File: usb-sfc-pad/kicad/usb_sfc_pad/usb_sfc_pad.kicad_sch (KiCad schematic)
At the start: 36 parts, among them IC101 PIC16F1459-ISS, J101 532610671, J102 532610271, J102 HEADER_6P-2.54, J103 532610271, J104 532610271, J105 532610271, SW101 SW_Pad, SW102 SW_Pad, SW103 SW_Pad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

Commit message: Add footprint SFC_Pad
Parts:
- SW101, SW102, SW103, SW104, SW105, SW106, SW107, SW108, SW109, SW110, SW111, SW112: footprint (none) -> Local:SFC_Pad_F_NoSolder_5.5mm
- renumbered J102 to J103, J103 to J104, J104 to J105, J105 to J106
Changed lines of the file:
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@@
 			)
 		)
-		(property "Footprint" ""
+		(property "Footprint" "Local:SFC_Pad_F_NoSolder_5.5mm"
 			(at 73.66 123.19 0)
 			(effects
@@
 			)
 		)
-		(property "Footprint" ""
+		(property "Footprint" "Local:SFC_Pad_F_NoSolder_5.5mm"
 			(at 110.49 123.19 0)
 			(effects
@@
 		(on_board yes)
 		(dnp no)
-		(property "Reference" "J105"
+		(property "Reference" "J106"
 			(at 256.032 118.364 90)
 			(effects
@@
 			(project "usb_sfc_pad"
 				(path "/7a50d412-cc3f-49bd-9754-262bb19f947d"
-					(reference "J105")
+					(reference "J106")
 					(unit 1)
 				)
@@
 		(on_board yes)
 		(dnp no)
-		(property "Reference" "J104"
+		(property "Reference" "J105"
 			(at 235.712 118.11 90)
 			(effects
@@
 			(project "usb_sfc_pad"
 				(path "/7a50d412-cc3f-49bd-9754-262bb19f947d"
-					(reference "J104")
+					(reference "J105")
 					(unit 1)
 				)
@@
 			)
 		)
-		(property "Footprint" ""
+		(property "Footprint" "Local:SFC_Pad_F_NoSolder_5.5mm"
 			(at 190.5 97.79 0)
 			(effects
@@
 			)
 		)
-		(property "Footprint" ""
+		(property "Footprint" "Local:SFC_Pad_F_NoSolder_5.5mm"
 			(at 38.1 123.19 0)
 			(effects
@@
 			)
 		)
-		(property "Footprint" ""
+		(property "Footprint" "Local:SFC_Pad_F_NoSolder_5.5mm"
 			(at 73.66 166.37 0)
 			(effects
@@
 		(on_board yes)
 		(dnp no)
-		(property "Reference" "J102"
+		(property "Reference" "J103"
 			(at 236.982 68.58 90)
 			(effects
@@
 			(project ""
 				(path "/7a50d412-cc3f-49bd-9754-262bb19f947d"
-					(reference "J102")
+					(reference "J103")
 					(unit 1)
 				)
@@
 			)
 		)
-		(property "Footprint" ""
+		(property "Footprint" "Local:SFC_Pad_F_NoSolder_5.5mm"
 			(at 260.35 93.98 0)
 			(effects
@@
 			)
 		)
-		(property "Footprint" ""
+		(property "Footprint" "Local:SFC_Pad_F_NoSolder_5.5mm"
 			(at 147.32 166.37 0)
 			(effects
@@
 			)
 		)
-		(property "Footprint" ""
+		(property "Footprint" "Local:SFC_Pad_F_NoSolder_5.5mm"
 			(at 38.1 166.37 0)
 			(effects
@@
 			)
 		)
-		(property "Footprint" ""
+		(property "Footprint" "Local:SFC_Pad_F_NoSolder_5.5mm"
 			(at 110.49 166.37 0)
 			(effects
@@
 		(on_board yes)
 		(dnp no)
-		(property "Reference" "J103"
+		(property "Reference" "J104"
 			(at 257.302 68.834 90)
 			(effects
@@
 			(project "usb_sfc_pad"
 				(path "/7a50d412-cc3f-49bd-9754-262bb19f947d"
-					(reference "J103")
+					(reference "J104")
 					(unit 1)
 				)
@@
 			)
 		)
-		(property "Footprint" ""
+		(property "Footprint" "Local:SFC_Pad_F_NoSolder_5.5mm"
 			(at 147.32 123.19 0)
 			(effects
@@
 			)
 		)
-		(property "Footprint" ""
+		(property "Footprint" "Local:SFC_Pad_F_NoSolder_5.5mm"
 			(at 190.5 140.97 0)
 			(effects
@@
 			)
 		)
-		(property "Footprint" ""
+		(property "Footprint" "Local:SFC_Pad_F_NoSolder_5.5mm"
 			(at 259.08 143.51 0)
 			(effects

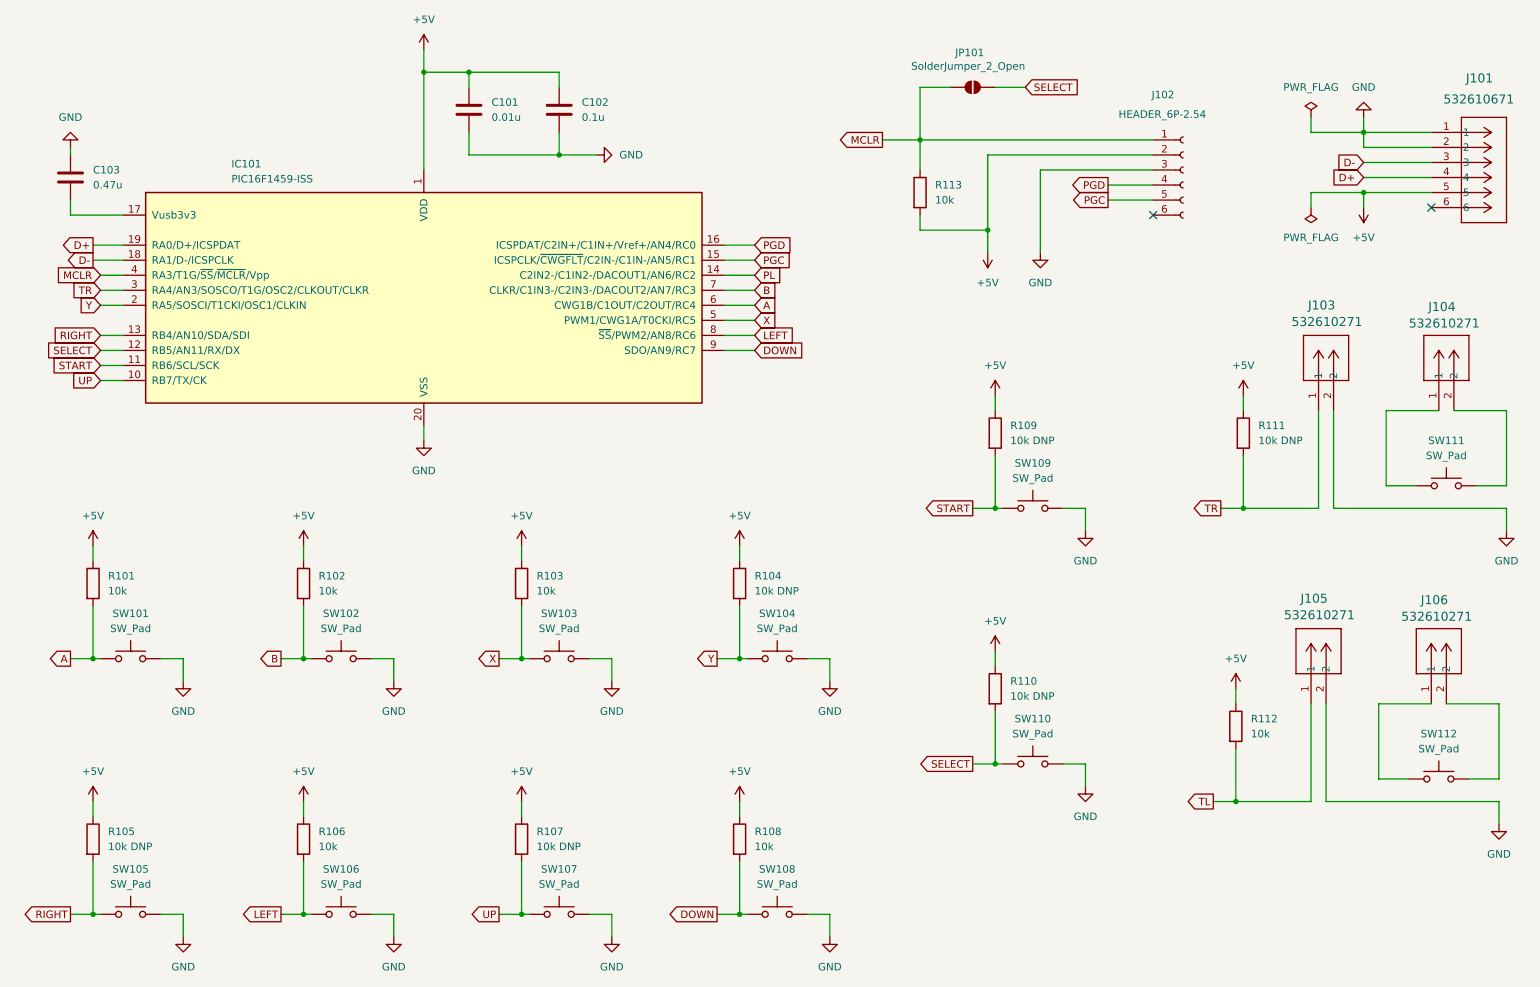
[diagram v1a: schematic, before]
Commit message: Add PCB
- Renumber SFC_Pad's pins
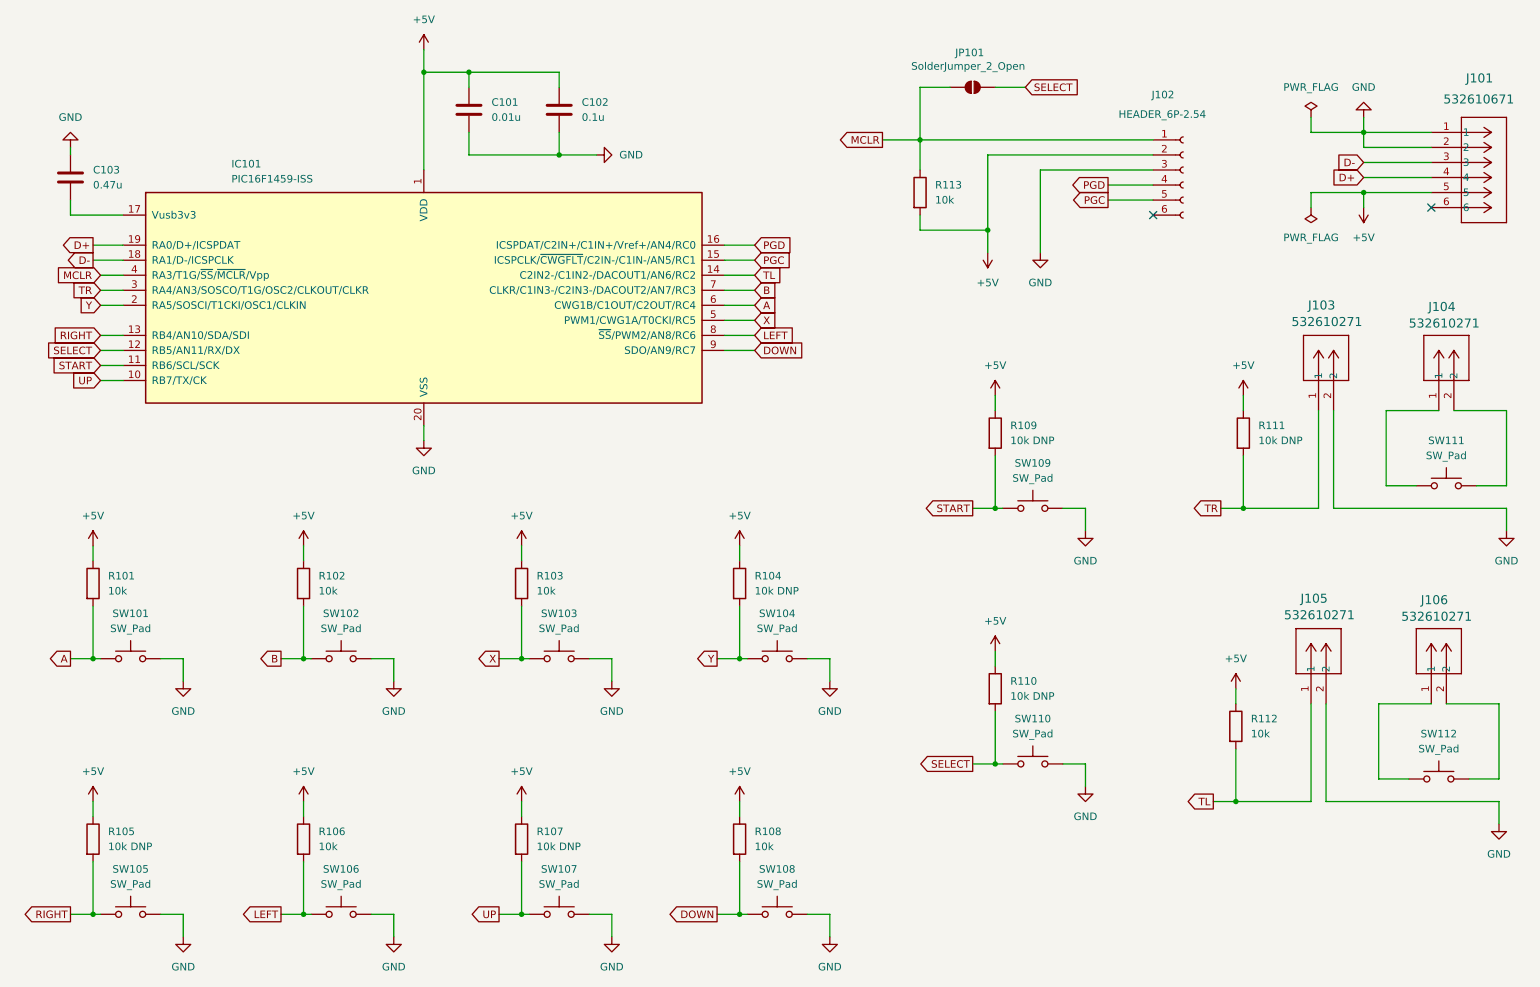
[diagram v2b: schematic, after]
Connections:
- net PL is gone; now on net TL: IC101.14 (C2IN2-/C1IN2-/DACOUT1/AN6/RC2)
- net A: now also SW101.2; no longer SW101.1
- net B: now also SW102.2; no longer SW102.1
- net GND: now also SW101.1, SW102.1, SW103.1, SW104.1, SW106.1; no longer SW101.2, SW102.2, SW103.2, SW104.2, SW106.2
- net LEFT: now also SW106.2; no longer SW106.1
- net X: now also SW103.2; no longer SW103.1
- net Y: now also SW104.2; no longer SW104.1
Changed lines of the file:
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@@
 		)
 	)
-	(global_label "PL"
+	(global_label "TL"
 		(shape input)
 		(at 143.51 63.5 0)
@@
 		)
 		(property "Intersheetrefs" "${INTERSHEET_REFS}"
-			(at 148.7933 63.5 0)
+			(at 148.4909 63.5 0)
 			(effects
 				(font
@@
 		(lib_id "Local:SW_Pad")
 		(at 73.66 128.27 0)
+		(mirror y)
 		(unit 1)
 		(exclude_from_sim no)
@@
 		(on_board yes)
 		(dnp no)
-		(fields_autoplaced yes)
 		(property "Reference" "SW102"
 			(at 73.66 120.65 0)
@@
 		(lib_id "Local:SW_Pad")
 		(at 110.49 128.27 0)
+		(mirror y)
 		(unit 1)
 		(exclude_from_sim no)
@@
 		(on_board yes)
 		(dnp no)
-		(fields_autoplaced yes)
 		(property "Reference" "SW103"
 			(at 110.49 120.65 0)
@@
 		(lib_id "Local:SW_Pad")
 		(at 38.1 128.27 0)
+		(mirror y)
 		(unit 1)
 		(exclude_from_sim no)
@@
 		(on_board yes)
 		(dnp no)
-		(fields_autoplaced yes)
 		(property "Reference" "SW101"
 			(at 38.1 120.65 0)
@@
 		(lib_id "Local:SW_Pad")
 		(at 73.66 171.45 0)
+		(mirror y)
 		(unit 1)
 		(exclude_from_sim no)
@@
 		(on_board yes)
 		(dnp no)
-		(fields_autoplaced yes)
 		(property "Reference" "SW106"
 			(at 73.66 163.83 0)
@@
 		(on_board yes)
 		(dnp no)
-		(fields_autoplaced yes)
 		(property "Reference" "SW108"
 			(at 147.32 163.83 0)
@@
 		(on_board yes)
 		(dnp no)
-		(fields_autoplaced yes)
 		(property "Reference" "SW105"
 			(at 38.1 163.83 0)
@@
 		(on_board yes)
 		(dnp no)
-		(fields_autoplaced yes)
 		(property "Reference" "SW107"
 			(at 110.49 163.83 0)
@@
 		(lib_id "Local:SW_Pad")
 		(at 147.32 128.27 0)
+		(mirror y)
 		(unit 1)
 		(exclude_from_sim no)
@@
 		(on_board yes)
 		(dnp no)
-		(fields_autoplaced yes)
 		(property "Reference" "SW104"
 			(at 147.32 120.65 0)

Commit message: Fix clearance in IC101 pads
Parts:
- IC101: footprint Package_SO:SSOP-20_5.3x7.2mm_P0.65mm -> Local:SSOP-20_5.3x7.2mm_P0.65mm
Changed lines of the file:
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@@
 			)
 		)
-		(property "Footprint" "Package_SO:SSOP-20_5.3x7.2mm_P0.65mm"
+		(property "Footprint" "Local:SSOP-20_5.3x7.2mm_P0.65mm"
 			(at 87.63 63.5 0)
 			(effects

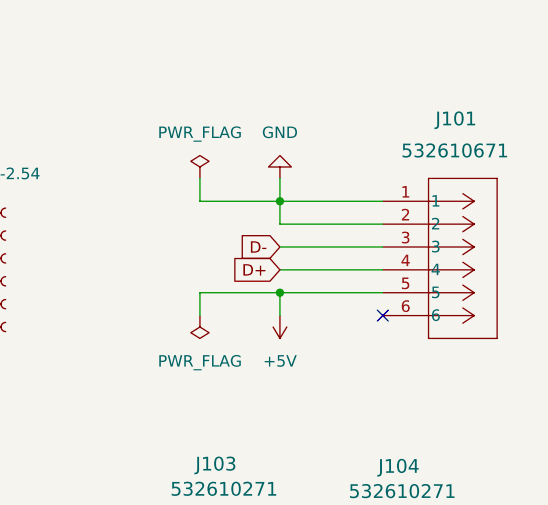
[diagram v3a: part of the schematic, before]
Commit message: Replace 532610671 with 532610571
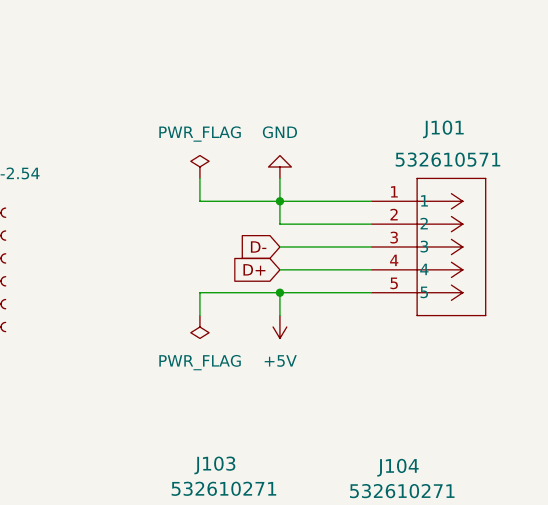
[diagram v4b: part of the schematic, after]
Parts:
- removed J101: 532610671, Local:CONN_532610001-SD_06_MOL, symbol Local:532610671
- added J101: 532610571, Local:CONN_532610001-SD_05_MOL, symbol Local:532610571
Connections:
- net +5V: now also J101.5
- net D+: now also J101.4
- net D-: now also J101.3
- net GND: now also J101.1, J101.2
- no-connect marks 2 -> 1
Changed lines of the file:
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@@
 		(at 210.82 53.34)
 	)
-	(no_connect
-		(at 257.81 52.07)
-	)
 	(wire
 		(pts
@@
 	(wire
 		(pts
-			(xy 257.81 49.53) (xy 246.38 49.53)
+			(xy 246.38 49.53) (xy 256.54 49.53)
 		)
 		(stroke
@@
 	(wire
 		(pts
-			(xy 246.38 44.45) (xy 257.81 44.45)
+			(xy 246.38 44.45) (xy 256.54 44.45)
 		)
 		(stroke
@@
 	(wire
 		(pts
-			(xy 246.38 46.99) (xy 257.81 46.99)
+			(xy 246.38 46.99) (xy 256.54 46.99)
 		)
 		(stroke
@@
 	(wire
 		(pts
-			(xy 257.81 41.91) (xy 246.38 41.91)
+			(xy 246.38 41.91) (xy 256.54 41.91)
 		)
 		(stroke
@@
 	(wire
 		(pts
-			(xy 257.81 39.37) (xy 246.38 39.37)
+			(xy 246.38 39.37) (xy 256.54 39.37)
 		)
 		(stroke
@@
 	)
 	(symbol
+		(lib_id "Local:532610571")
+		(at 256.54 39.37 0)
+		(unit 1)
+		(exclude_from_sim no)
+		(in_bom yes)
+		(on_board yes)
+		(dnp no)
+		(property "Reference" "J101"
+			(at 262.382 31.242 0)
+			(effects
+				(font
+					(size 1.524 1.524)
+				)
+				(justify left)
+			)
+		)
+		(property "Value" "532610571"
+			(at 259.08 34.798 0)
+			(effects
+				(font
+					(size 1.524 1.524)
+				)
+				(justify left)
+			)
+		)
+		(property "Footprint" "Local:CONN_532610001-SD_05_MOL"
+			(at 264.414 54.356 0)
+			(effects
+				(font
+					(size 1.27 1.27)
+				)
+				(hide yes)
+			)
+		)
+		(property "Datasheet" "https://www.molex.com/en-us/products/part-detail-pdf/532610571?display=pdf"
+			(at 265.43 57.15 0)
+			(effects
+				(font
+					(size 1.27 1.27)
+				)
+				(hide yes)
+			)
+		)
+		(property "Description" ""
+			(at 256.54 39.37 0)
+			(effects
+				(font
+					(size 1.27 1.27)
+				)
+				(hide yes)
+			)
+		)
+		(pin "4"
+		)
+		(pin "5"
+		)
+		(pin "1"
+		)
+		(pin "3"
+		)
+		(pin "2"
+		)
+		(instances
+			(project ""
+				(path "/7a50d412-cc3f-49bd-9754-262bb19f947d"
+					(reference "J101")
+					(unit 1)
+				)
+			)
+		)
+	)
+	(symbol
 		(lib_id "power:GND")
 		(at 246.38 36.83 0)
@@
 					(unit 1)
 				)
-			)
-		)
-	)
-	(symbol
-		(lib_id "Local:532610671")
-		(at 257.81 39.37 0)
-		(unit 1)
-		(exclude_from_sim no)
-		(in_bom yes)
-		(on_board yes)
-		(dnp no)
-		(property "Reference" "J101"
-			(at 263.652 30.226 0)
-			(effects
-				(font
-					(size 1.524 1.524)
-				)
-				(justify left)
-			)
-		)
-		(property "Value" "532610671"
-			(at 259.842 33.782 0)
-			(effects
-				(font
-					(size 1.524 1.524)
-				)
-				(justify left)
-			)
-		)
-		(property "Footprint" "Local:CONN_532610001-SD_06_MOL"
-			(at 266.7 56.896 0)
-			(effects
-				(font
-					(size 1.27 1.27)
-					(italic yes)
-				)
-				(hide yes)
-			)
-		)
-		(property "Datasheet" "https://www.molex.com/en-us/products/part-detail-pdf/532610671?display=pdf"
-			(at 264.922 59.944 0)
-			(effects
-				(font
-					(size 1.27 1.27)
-					(italic yes)
-				)
-				(hide yes)
-			)
-		)
-		(property "Description" ""
-			(at 257.81 39.37 0)
-			(effects
-				(font
-					(size 1.27 1.27)
-				)
-				(hide yes)
-			)
-		)
-		(pin "1"
-		)
-		(pin "2"
-		)
-		(pin "5"
-		)
-		(pin "6"
-		)
-		(pin "3"
-		)
-		(pin "4"
-		)
-		(instances
-			(project ""
-				(path "/7a50d412-cc3f-49bd-9754-262bb19f947d"
-					(reference "J101")
-					(unit 1)
-				)

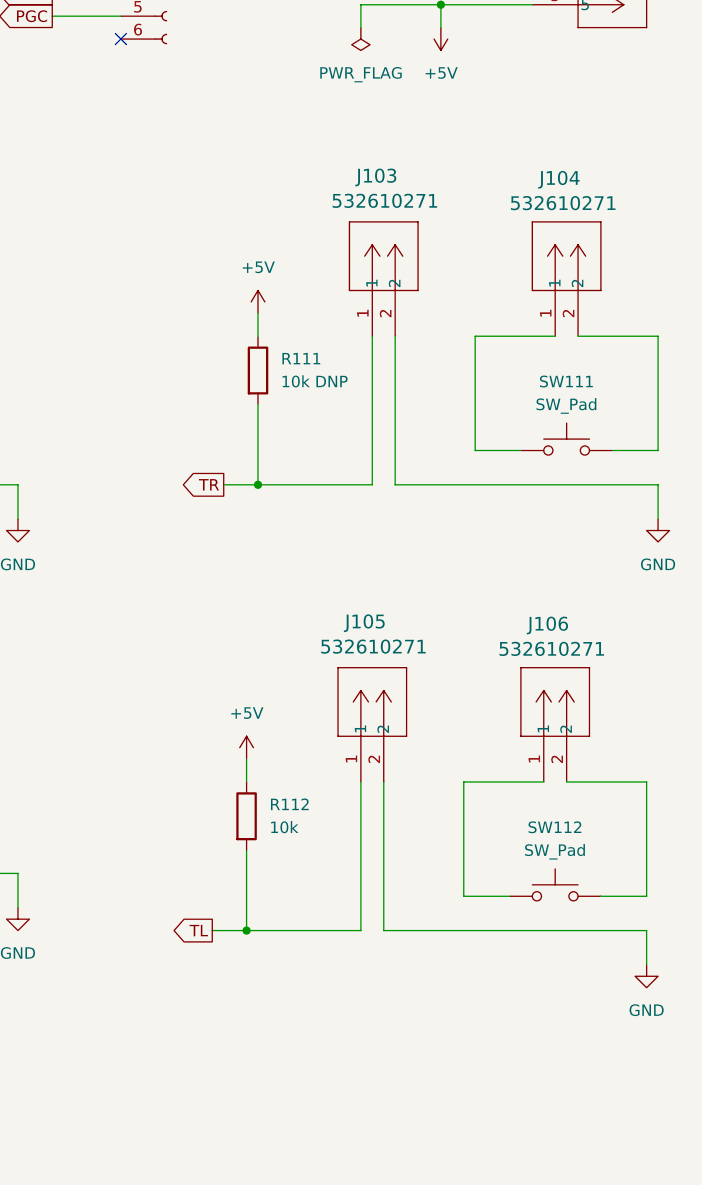
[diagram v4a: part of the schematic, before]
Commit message: Replace right-angle 2pins with vertical ones
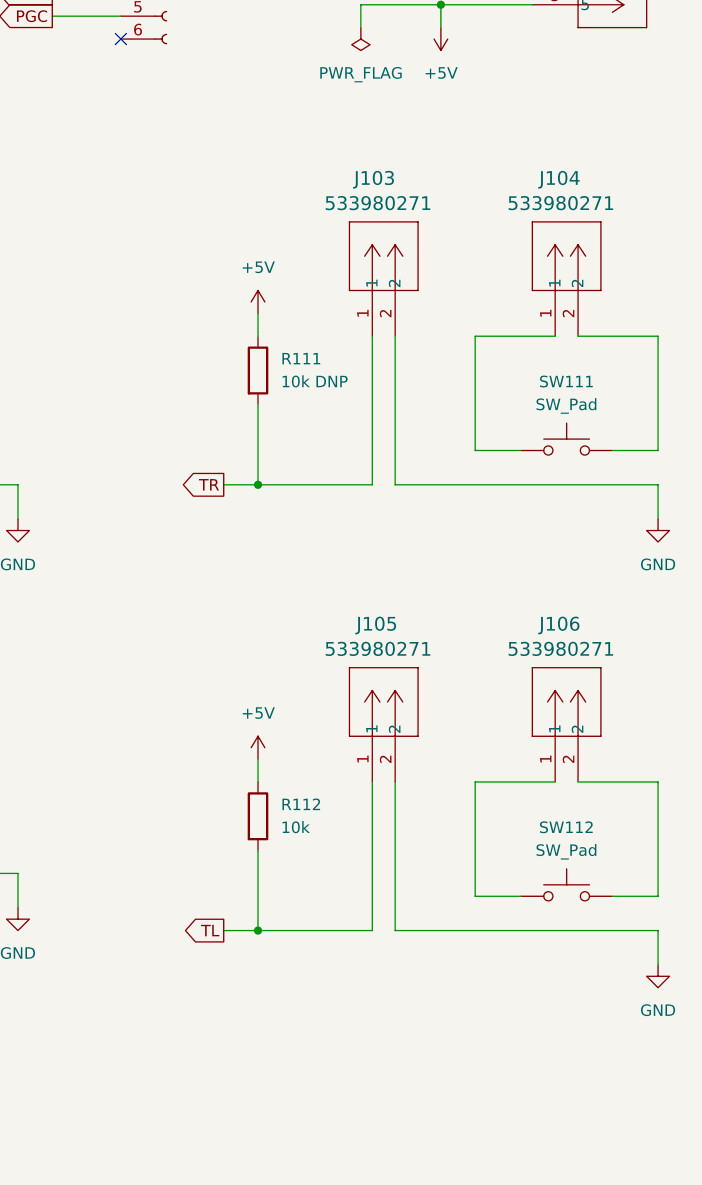
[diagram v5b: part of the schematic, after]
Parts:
- removed J103, J104, J105, J106: 532610271, Local:CONN_532610001-SD_02_MOL, symbol Local:532610271
- added J103, J104, J105, J106: 533980271, Local:CONN02_533980271_MOL, symbol Local:533980271
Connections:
- net GND: now also J103.2, J105.2
- net TL: now also J105.1
- net TR: now also J103.1
- net at SW112.1: now also J106.1
- net at SW112.2: now also J106.2
- net at SW111.1: now also J104.1
- net at SW111.2: now also J104.2
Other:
- moved on the sheet: R112, SW112
